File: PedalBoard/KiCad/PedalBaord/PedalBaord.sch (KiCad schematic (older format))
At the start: 17 parts

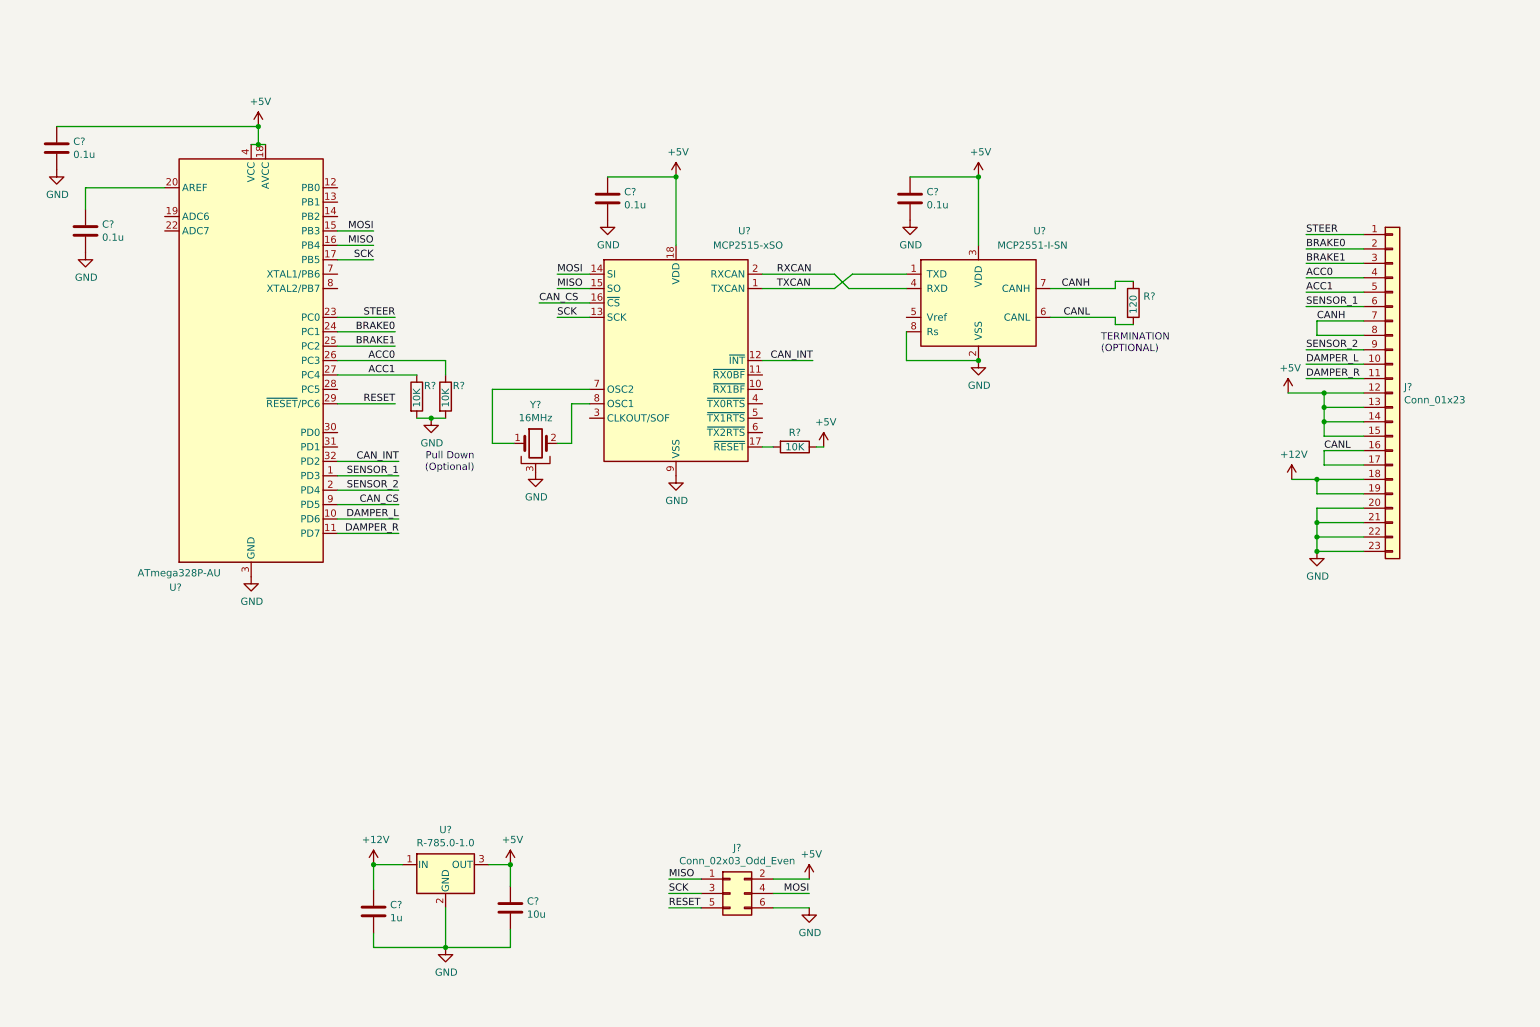
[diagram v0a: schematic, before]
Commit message: update schematic
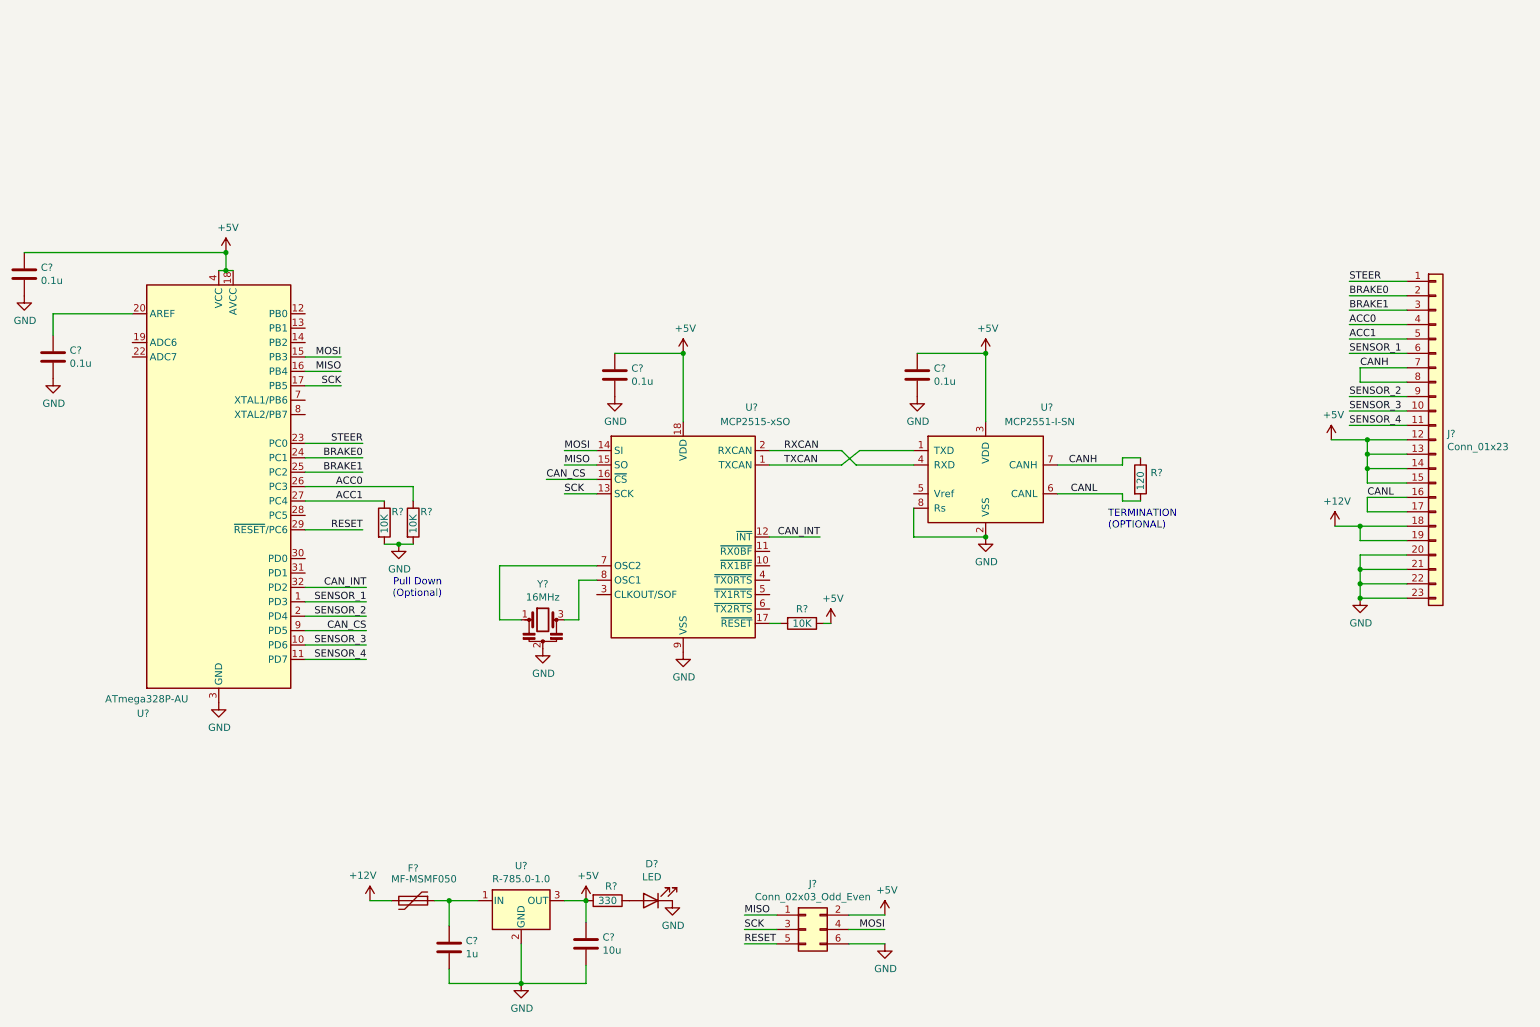
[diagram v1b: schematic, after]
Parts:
- removed C? (x2): 0.1u, symbol Device:C
- removed C?: 1u, symbol Device:C
- removed J?: Conn_02x03_Odd_Even, symbol Connector_Generic:Conn_02x03_Odd_Even
- removed R?: 10K, symbol Device:R
- removed R?: 120, symbol Device:R
- removed U?: MCP2515-xSO, Package_SO:SOIC-18W_7.5x11.6mm_P1.27mm, symbol Interface_CAN_LIN:MCP2515-xSO
- removed U?: MCP2551-I-SN, Package_SO:SOIC-8_3.9x4.9mm_P1.27mm, symbol Interface_CAN_LIN:MCP2551-I-SN
- removed Y?: 16MHz, symbol Device:Crystal_GND3
- added C?: 1u, symbol Device:C
- added C? (x2): 0.1u, symbol Device:C
- added D?: LED, symbol Device:LED
- added F?: MF-MSMF050, symbol Device:Polyfuse
- added J?: Conn_02x03_Odd_Even, symbol Connector_Generic:Conn_02x03_Odd_Even
- added R?: 330, symbol Device:R
- added R?: 10K, symbol Device:R
- added R?: 120, symbol Device:R
- added U?: MCP2515-xSO, Package_SO:SOIC-18W_7.5x11.6mm_P1.27mm, symbol Interface_CAN_LIN:MCP2515-xSO
- added U?: MCP2551-I-SN, Package_SO:SOIC-8_3.9x4.9mm_P1.27mm, symbol Interface_CAN_LIN:MCP2551-I-SN
- added Y?: 16MHz, symbol Device:Resonator
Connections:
- net +12V: now also F?.2; no longer U?.1 (IN)
- net +5V: now also C?.1, C?.1, J?.2 (Pin_2), R?.1, R?.2, U?.18 (VDD), U?.3 (VDD)
- net CANH: now also R?.1, U?.7 (CANH)
- net CANL: now also R?.2, U?.6 (CANL)
- net CAN_CS: now also U?.16 (~CS)
- net CAN_INT: now also U?.12 (~INT)
- net GND: now also C?.2, C?.2, C?.2, D?.1 (K), J?.6 (Pin_6), U?.2 (VSS), U?.8 (Rs), U?.9 (VSS), Y?.2
- net MISO: now also J?.1 (Pin_1), U?.15 (SO)
- net MOSI: now also J?.4 (Pin_4), U?.14 (SI)
- net RESET: now also J?.5 (Pin_5)
- net RXCAN: now also U?.2 (RXCAN), U?.4 (RXD)
- net SCK: now also J?.3 (Pin_3), U?.13 (SCK)
- net TXCAN: now also U?.1 (TXCAN), U?.1 (TXD)
- net DAMPER_L renamed SENSOR_3
- net DAMPER_R renamed SENSOR_4
- new net: U?.7 (OSC2), Y?.1
- new net: U?.8 (OSC1), Y?.3
- new net: C?.1, F?.1, U?.1 (IN)
- new net: D?.2 (A), R?.1
- new net: R?.2, U?.17 (~RESET)
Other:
- moved on the sheet: C?, J?, R?, U?

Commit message: first layout design
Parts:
- added C7: 0.1u, Capacitor_SMD:C_0603_1608Metric_Pad1.08x0.95mm_HandSolder, symbol Device:C
- added U5: MCP3008, Package_SO:SOIC-16_3.9x9.9mm_P1.27mm, symbol Analog_ADC:MCP3008
- C1, C2, C3, C4, C5, C6: renamed from C?; footprint (none) -> Capacitor_SMD:C_0603_1608Metric_Pad1.08x0.95mm_HandSolder
- D1: renamed from D?; footprint (none) -> LED_SMD:LED_0603_1608Metric_Pad1.05x0.95mm_HandSolder
- F1: renamed from F?; footprint (none) -> Fuse:Fuse_1812_4532Metric_Pad1.30x3.40mm_HandSolder
- J1: renamed from J?; footprint (none) -> Connector_PinHeader_2.54mm:PinHeader_2x03_P2.54mm_Vertical
- J2: renamed from J?; footprint (none) -> AERO_CUSTOM:TE_1-770669-1_23pin_Horizontal
- R1, R2, R3, R4, R5: renamed from R?; footprint (none) -> Resistor_SMD:R_0603_1608Metric_Pad0.98x0.95mm_HandSolder
- Y1: renamed from Y?; footprint (none) -> AERO_CUSTOM:Resonator_SMD_muRata_CSTxExxV-3Pin_3.0x1.1mm_HandSoldering
- gave numbers to parts that had none: 4
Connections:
- net +12V: now also J2.15 (Pin_15), J2.23 (Pin_23); no longer J2.18 (Pin_18), J2.19 (Pin_19)
- net +5V: now also J2.5 (Pin_5), J2.6 (Pin_6), J2.7 (Pin_7), J2.8 (Pin_8), C7.1, U5.15 (Vref), U5.16 (Vdd); no longer J2.12 (Pin_12), J2.13 (Pin_13), J2.14 (Pin_14), J2.15 (Pin_15)
- net ACC0: now also J2.9 (Pin_9), R1.1, U1.27 (PC4); no longer J2.4 (Pin_4), R2.1, U1.26 (PC3)
- net ACC1: now also J2.10 (Pin_10), R2.1, U1.26 (PC3); no longer J2.5 (Pin_5), R1.1, U1.27 (PC4)
- net BRAKE0: now also J2.16 (Pin_16), U1.25 (PC2); no longer J2.2 (Pin_2), U1.24 (PC1)
- net BRAKE1: now also J2.17 (Pin_17), U1.24 (PC1); no longer J2.3 (Pin_3), U1.25 (PC2)
- net GND: now also J2.1 (Pin_1), J2.2 (Pin_2), J2.3 (Pin_3), J2.4 (Pin_4), C7.2, U5.14 (AGND), U5.9 (DGND); no longer J2.20 (Pin_20), J2.21 (Pin_21), J2.22 (Pin_22), J2.23 (Pin_23)
- net MISO: now also U5.12 (Dout)
- net MOSI: now also U5.11 (Din)
- net SCK: now also U5.13 (CLK)
- net SENSOR_1: no longer J2.6 (Pin_6)
- net SENSOR_2: no longer J2.9 (Pin_9)
- net SENSOR_3: no longer J2.10 (Pin_10)
- net SENSOR_4: no longer J2.11 (Pin_11)
- net STEER: now also J2.11 (Pin_11); no longer J2.1 (Pin_1)
- net ADC_CS: now reaches U1.13 (PB1)
- net ADC_CS: now also U5.10 (~CS~/SHDN)
- net CANH renamed CAN+
- net CAN+: now also J2.13 (Pin_13), J2.21 (Pin_21); no longer J2.7 (Pin_7), J2.8 (Pin_8)
- net CANL renamed CAN-
- net CAN-: now also J2.14 (Pin_14), J2.22 (Pin_22); no longer J2.16 (Pin_16), J2.17 (Pin_17)
- new net DAMPER_L: J2.12 (Pin_12), U5.3 (CH2)
- new net DAMPER_R: J2.18 (Pin_18), U5.4 (CH3)
- new net WHEEL_L: J2.20 (Pin_20), U5.1 (CH0)
- new net WHEEL_R: J2.19 (Pin_19), U5.2 (CH1)
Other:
- moved on the sheet: C5, C6, J2, R4, R5, U3, U4, Y1
